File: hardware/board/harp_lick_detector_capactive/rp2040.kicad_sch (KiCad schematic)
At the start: 5 parts

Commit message: update analog front end
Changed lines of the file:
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@@
-    (effects (font (size 1.27 1.27)) (justify left))
-  )
-  (hierarchical_label "POCI" (shape input) (at 257.81 64.77 0)
     (effects (font (size 1.27 1.27)) (justify left))
   )
@@
     (effects (font (size 1.27 1.27)) (justify left))
   )
+  (hierarchical_label "ADC" (shape input) (at 257.81 125.73 0)
+    (effects (font (size 1.27 1.27)) (justify left))
+  )

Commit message: assign sch components partial
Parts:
- J2: renamed from J?; value USB_C_Receptacle_USB2.0 -> (none)
- R? (x2): value 5K1 -> (none)
- U7: renamed from U?; value W25Q128JVS -> (none); footprint Package_SO:SOIC-8_5.23x5.23mm_P1.27mm -> (none)
- U8: renamed from U?; value RP2040 -> (none); footprint RP2040_minimal:RP2040-QFN-56 -> (none)
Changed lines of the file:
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@@
     (in_bom yes) (on_board yes)
     (property "Reference" "R?" (id 0) (at 54.61 76.2 90))
-    (property "Value" "5K1" (id 1) (at 59.69 76.2 90))
+    (property "Value" "" (id 1) (at 59.69 76.2 90))
     (property "Footprint" "" (id 2) (at 57.15 80.518 90)
       (effects (font (size 1.27 1.27)) hide)
@@
   (symbol (lib_id "pi_pico:RP2040") (at 193.04 95.25 0) (unit 1)
     (in_bom yes) (on_board yes) (fields_autoplaced)
-    (property "Reference" "U?" (id 0) (at 195.0594 146.05 0)
+    (property "Reference" "U8" (id 0) (at 195.0594 146.05 0)
       (effects (font (size 1.27 1.27)) (justify left))
     )
-    (property "Value" "RP2040" (id 1) (at 195.0594 148.59 0)
+    (property "Value" "" (id 1) (at 195.0594 148.59 0)
       (effects (font (size 1.27 1.27)) (justify left))
     )
-    (property "Footprint" "RP2040_minimal:RP2040-QFN-56" (id 2) (at 173.99 95.25 0)
+    (property "Footprint" "" (id 2) (at 173.99 95.25 0)
       (effects (font (size 1.27 1.27)) hide)
     )
@@
   (symbol (lib_id "Memory_Flash:W25Q128JVS") (at 140.97 177.8 0) (unit 1)
     (in_bom yes) (on_board yes) (fields_autoplaced)
-    (property "Reference" "U?" (id 0) (at 142.9894 165.1 0)
+    (property "Reference" "U7" (id 0) (at 142.9894 165.1 0)
       (effects (font (size 1.27 1.27)) (justify left))
     )
-    (property "Value" "W25Q128JVS" (id 1) (at 142.9894 167.64 0)
+    (property "Value" "" (id 1) (at 142.9894 167.64 0)
       (effects (font (size 1.27 1.27)) (justify left))
     )
-    (property "Footprint" "Package_SO:SOIC-8_5.23x5.23mm_P1.27mm" (id 2) (at 140.97 177.8 0)
+    (property "Footprint" "" (id 2) (at 140.97 177.8 0)
       (effects (font (size 1.27 1.27)) hide)
     )
@@
   (symbol (lib_id "Connector:USB_C_Receptacle_USB2.0") (at 35.56 88.9 0) (unit 1)
     (in_bom yes) (on_board yes) (fields_autoplaced)
-    (property "Reference" "J?" (id 0) (at 35.56 66.04 0))
-    (property "Value" "USB_C_Receptacle_USB2.0" (id 1) (at 35.56 68.58 0))
+    (property "Reference" "J2" (id 0) (at 35.56 66.04 0))
+    (property "Value" "" (id 1) (at 35.56 68.58 0))
     (property "Footprint" "" (id 2) (at 39.37 88.9 0)
       (effects (font (size 1.27 1.27)) hide)
@@
     (in_bom yes) (on_board yes)
     (property "Reference" "R?" (id 0) (at 54.61 83.82 90))
-    (property "Value" "5K1" (id 1) (at 59.69 83.82 90))
+    (property "Value" "" (id 1) (at 59.69 83.82 90))
     (property "Footprint" "" (id 2) (at 57.15 83.058 90)
       (effects (font (size 1.27 1.27)) hide)

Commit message: assign more sch components
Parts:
- R? (x2): Link (none) -> https://www.digikey.com/en/products/detail/panasonic-electr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; Manufacturer (none) -> Panasonic Electronic Components; Manufacturer Number (none) -> ERJ-UP3F5101V; Tolerance (none) -> 1%
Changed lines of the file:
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@@
       (effects (font (size 1.27 1.27)) hide)
     )
-    (property "Datasheet" "~" (id 3) (at 57.15 78.74 0)
+    (property "Datasheet" "https://api.pim.na.industrial.panasonic.com/file_stream/main/fileversion/4484" (id 3) (at 57.15 78.74 0)
+      (effects (font (size 1.27 1.27)) hide)
+    )
+    (property "Link" "https://www.digikey.com/en/products/detail/panasonic-electronic-components/ERJ-UP3F5101V/12093051" (id 4) (at 57.15 78.74 0)
+      (effects (font (size 1.27 1.27)) hide)
+    )
+    (property "Manufacturer" "Panasonic Electronic Components" (id 5) (at 57.15 78.74 0)
+      (effects (font (size 1.27 1.27)) hide)
+    )
+    (property "Manufacturer Number" "ERJ-UP3F5101V" (id 6) (at 57.15 78.74 0)
+      (effects (font (size 1.27 1.27)) hide)
+    )
+    (property "Tolerance" "1%" (id 7) (at 57.15 78.74 0)
       (effects (font (size 1.27 1.27)) hide)
     )
@@
       (effects (font (size 1.27 1.27)) hide)
     )
-    (property "Datasheet" "~" (id 3) (at 57.15 81.28 0)
+    (property "Datasheet" "https://api.pim.na.industrial.panasonic.com/file_stream/main/fileversion/4484" (id 3) (at 57.15 81.28 0)
+      (effects (font (size 1.27 1.27)) hide)
+    )
+    (property "Link" "https://www.digikey.com/en/products/detail/panasonic-electronic-components/ERJ-UP3F5101V/12093051" (id 4) (at 57.15 81.28 0)
+      (effects (font (size 1.27 1.27)) hide)
+    )
+    (property "Manufacturer" "Panasonic Electronic Components" (id 5) (at 57.15 81.28 0)
+      (effects (font (size 1.27 1.27)) hide)
+    )
+    (property "Manufacturer Number" "ERJ-UP3F5101V" (id 6) (at 57.15 81.28 0)
+      (effects (font (size 1.27 1.27)) hide)
+    )
+    (property "Tolerance" "1%" (id 7) (at 57.15 81.28 0)
       (effects (font (size 1.27 1.27)) hide)
     )
@@
   (symbol (lib_id "power:VBUS") (at 52.07 72.39 0) (unit 1)
     (in_bom yes) (on_board yes) (fields_autoplaced)
-    (property "Reference" "#PWR?" (id 0) (at 52.07 76.2 0)
+    (property "Reference" "#PWR0135" (id 0) (at 52.07 76.2 0)
       (effects (font (size 1.27 1.27)) hide)
     )
@@
   (symbol (lib_id "power:GND") (at 63.5 80.01 90) (unit 1)
     (in_bom yes) (on_board yes) (fields_autoplaced)
-    (property "Reference" "#PWR?" (id 0) (at 69.85 80.01 0)
+    (property "Reference" "#PWR0134" (id 0) (at 69.85 80.01 0)
       (effects (font (size 1.27 1.27)) hide)
     )

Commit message: assign more components
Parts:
- added D?: (no value), symbol Device:LED
- added FID? (x3): (no value), symbol Mechanical:Fiducial
- J2: Link (none) -> https://www.digikey.com/en/products/detail/amphenol-cs-comm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; Manufacturer (none) -> Amphenol ICC (Commercial Products); Manufacturer Number (none) -> 12401610E4#2A
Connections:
- net GND: now also J2.A1 (GND), J2.A12 (GND), J2.B1 (GND), J2.B12 (GND), J2.S1 (SHIELD)
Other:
- note added: "TODO: crystal TODO: 3v3 Serial Port TODO: reset TODO: SWD port TODO: Harp audio jack TODO: USB Ground Loop Breaker"
- note removed: "TODO: Don't forget Fiducials."
- note removed: "TODO: crystal TODO: reset TODO: SWD port TODO: Harp audio jack"
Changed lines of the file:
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@@
   (junction (at 52.07 87.63) (diameter 0) (color 0 0 0 0)
+  )
+  (junction (at 31.75 113.03) (diameter 0) (color 0 0 0 0)
   )
   (junction (at 52.07 92.71) (diameter 0) (color 0 0 0 0)
@@
   (no_connect (at 50.8 101.6))
   (no_connect (at 50.8 104.14))
+  (wire (pts (xy 35.56 111.76) (xy 35.56 113.03))
+    (stroke (width 0) (type default) (color 0 0 0 0))
+  )
   (wire (pts (xy 60.96 78.74) (xy 62.23 78.74))
     (stroke (width 0) (type default) (color 0 0 0 0))
@@
     (stroke (width 0) (type default) (color 0 0 0 0))
   )
+  (wire (pts (xy 27.94 111.76) (xy 27.94 113.03))
+    (stroke (width 0) (type default) (color 0 0 0 0))
+  )
   (wire (pts (xy 52.07 93.98) (xy 50.8 93.98))
     (stroke (width 0) (type default) (color 0 0 0 0))
@@
     (stroke (width 0) (type default) (color 0 0 0 0))
   )
+  (wire (pts (xy 35.56 113.03) (xy 31.75 113.03))
+    (stroke (width 0) (type default) (color 0 0 0 0))
+  )
   (wire (pts (xy 62.23 81.28) (xy 62.23 80.01))
     (stroke (width 0) (type default) (color 0 0 0 0))
@@
     (stroke (width 0) (type default) (color 0 0 0 0))
   )
+  (wire (pts (xy 27.94 113.03) (xy 31.75 113.03))
+    (stroke (width 0) (type default) (color 0 0 0 0))
+  )
   (wire (pts (xy 52.07 72.39) (xy 52.07 73.66))
     (stroke (width 0) (type default) (color 0 0 0 0))
@@
     (stroke (width 0) (type default) (color 0 0 0 0))
   )
+  (wire (pts (xy 31.75 113.03) (xy 31.75 114.3))
+    (stroke (width 0) (type default) (color 0 0 0 0))
+  )
   (wire (pts (xy 50.8 86.36) (xy 52.07 86.36))
     (stroke (width 0) (type default) (color 0 0 0 0))
@@
     (stroke (width 0) (type default) (color 0 0 0 0))
   )
-  (text "TODO: crystal\nTODO: reset\nTODO: SWD port\nTODO: Harp audio jack"
+  (text "TODO: crystal\nTODO: 3v3 Serial Port\nTODO: reset\nTODO: SWD port\nTODO: Harp audio jack\nTODO: USB Ground Loop Breaker"
     (at 20.32 184.15 0)
-    (effects (font (size 1.27 1.27)) (justify left bottom))
-  )
-  (text "TODO: Don't forget Fiducials." (at 251.46 17.78 0)
     (effects (font (size 1.27 1.27)) (justify left bottom))
   )
@@
     (pin "1")
     (pin "2")
+  )
+  (symbol (lib_id "power:GND") (at 31.75 114.3 0) (unit 1)
+    (in_bom yes) (on_board yes) (fields_autoplaced)
+    (property "Reference" "#PWR?" (id 0) (at 31.75 120.65 0)
+      (effects (font (size 1.27 1.27)) hide)
+    )
+    (property "Value" "GND" (id 1) (at 34.29 115.5699 0)
+      (effects (font (size 1.27 1.27)) (justify left))
+    )
+    (property "Footprint" "" (id 2) (at 31.75 114.3 0)
+      (effects (font (size 1.27 1.27)) hide)
+    )
+    (property "Datasheet" "" (id 3) (at 31.75 114.3 0)
+      (effects (font (size 1.27 1.27)) hide)
+    )
+    (pin "1")
   )
   (symbol (lib_id "pi_pico:RP2040") (at 193.04 95.25 0) (unit 1)
@@
     (pin "9")
   )
+  (symbol (lib_id "Mechanical:Fiducial") (at 17.78 24.13 0) (unit 1)
+    (in_bom yes) (on_board yes) (fields_autoplaced)
+    (property "Reference" "FID?" (id 0) (at 20.32 22.8599 0)
+      (effects (font (size 1.27 1.27)) (justify left))
+    )
+    (property "Value" "" (id 1) (at 20.32 25.3999 0)
+      (effects (font (size 1.27 1.27)) (justify left))
+    )
+    (property "Footprint" "" (id 2) (at 17.78 24.13 0)
+      (effects (font (size 1.27 1.27)) hide)
+    )
+    (property "Datasheet" "~" (id 3) (at 17.78 24.13 0)
+      (effects (font (size 1.27 1.27)) hide)
+    )
+  )
+  (symbol (lib_id "Mechanical:Fiducial") (at 17.78 29.21 0) (unit 1)
+    (in_bom yes) (on_board yes) (fields_autoplaced)
+    (property "Reference" "FID?" (id 0) (at 20.32 27.9399 0)
+      (effects (font (size 1.27 1.27)) (justify left))
+    )
+    (property "Value" "" (id 1) (at 20.32 30.4799 0)
+      (effects (font (size 1.27 1.27)) (justify left))
+    )
+    (property "Footprint" "" (id 2) (at 17.78 29.21 0)
+      (effects (font (size 1.27 1.27)) hide)
+    )
+    (property "Datasheet" "~" (id 3) (at 17.78 29.21 0)
+      (effects (font (size 1.27 1.27)) hide)
+    )
+  )
   (symbol (lib_id "Memory_Flash:W25Q128JVS") (at 140.97 177.8 0) (unit 1)
     (in_bom yes) (on_board yes) (fields_autoplaced)
@@
     )
     (property "Datasheet" "https://www.usb.org/sites/default/files/documents/usb_type-c.zip" (id 3) (at 39.37 88.9 0)
+      (effects (font (size 1.27 1.27)) hide)
+    )
+    (property "Link" "https://www.digikey.com/en/products/detail/amphenol-cs-commercial-products/12401610E4-2A/5775519" (id 4) (at 35.56 88.9 0)
+      (effects (font (size 1.27 1.27)) hide)
+    )
+    (property "Manufacturer" "Amphenol ICC (Commercial Products)" (id 5) (at 35.56 88.9 0)
+      (effects (font (size 1.27 1.27)) hide)
+    )
+    (property "Manufacturer Number" "12401610E4#2A" (id 6) (at 35.56 88.9 0)
       (effects (font (size 1.27 1.27)) hide)
     )
@@
     (pin "1")
   )
+  (symbol (lib_id "Mechanical:Fiducial") (at 17.78 19.05 0) (unit 1)
+    (in_bom yes) (on_board yes) (fields_autoplaced)
+    (property "Reference" "FID?" (id 0) (at 20.32 17.7799 0)
+      (effects (font (size 1.27 1.27)) (justify left))
+    )
+    (property "Value" "" (id 1) (at 20.32 20.3199 0)
+      (effects (font (size 1.27 1.27)) (justify left))
+    )
+    (property "Footprint" "" (id 2) (at 17.78 19.05 0)
+      (effects (font (size 1.27 1.27)) hide)
+    )
+    (property "Datasheet" "~" (id 3) (at 17.78 19.05 0)
+      (effects (font (size 1.27 1.27)) hide)
+    )
+  )
   (symbol (lib_id "power:GND") (at 63.5 80.01 90) (unit 1)
     (in_bom yes) (on_board yes) (fields_autoplaced)
@@
     (pin "1")
   )
+  (symbol (lib_id "Device:LED") (at 270.51 81.28 90) (unit 1)
+    (in_bom yes) (on_board yes) (fields_autoplaced)
+    (property "Reference" "D?" (id 0) (at 274.32 81.5974 90)
+      (effects (font (size 1.27 1.27)) (justify right))
+    )
+    (property "Value" "" (id 1) (at 274.32 84.1374 90)
+      (effects (font (size 1.27 1.27)) (justify right))
+    )
+    (property "Footprint" "" (id 2) (at 270.51 81.28 0)
+      (effects (font (size 1.27 1.27)) hide)
+    )
+    (property "Datasheet" "~" (id 3) (at 270.51 81.28 0)
+      (effects (font (size 1.27 1.27)) hide)
+    )
+    (pin "1")
+    (pin "2")
+  )
 )

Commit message: assign more components
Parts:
- U7: Link (none) -> https://www.digikey.com/en/products/detail/winbond-electron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; Manufacturer (none) -> Winbond Electronics; Manufacturer Number (none) -> W25Q128JVSIQ TR
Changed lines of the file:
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@@
+      (effects (font (size 1.27 1.27)) hide)
+    )
+    (property "Link" "https://www.digikey.com/en/products/detail/winbond-electronics/W25Q128JVSIQ-TR/5803944" (id 4) (at 140.97 177.8 0)
+      (effects (font (size 1.27 1.27)) hide)
+    )
+    (property "Manufacturer" "Winbond Electronics" (id 5) (at 140.97 177.8 0)
+      (effects (font (size 1.27 1.27)) hide)
+    )
+    (property "Manufacturer Number" "W25Q128JVSIQ TR" (id 6) (at 140.97 177.8 0)
       (effects (font (size 1.27 1.27)) hide)
     )

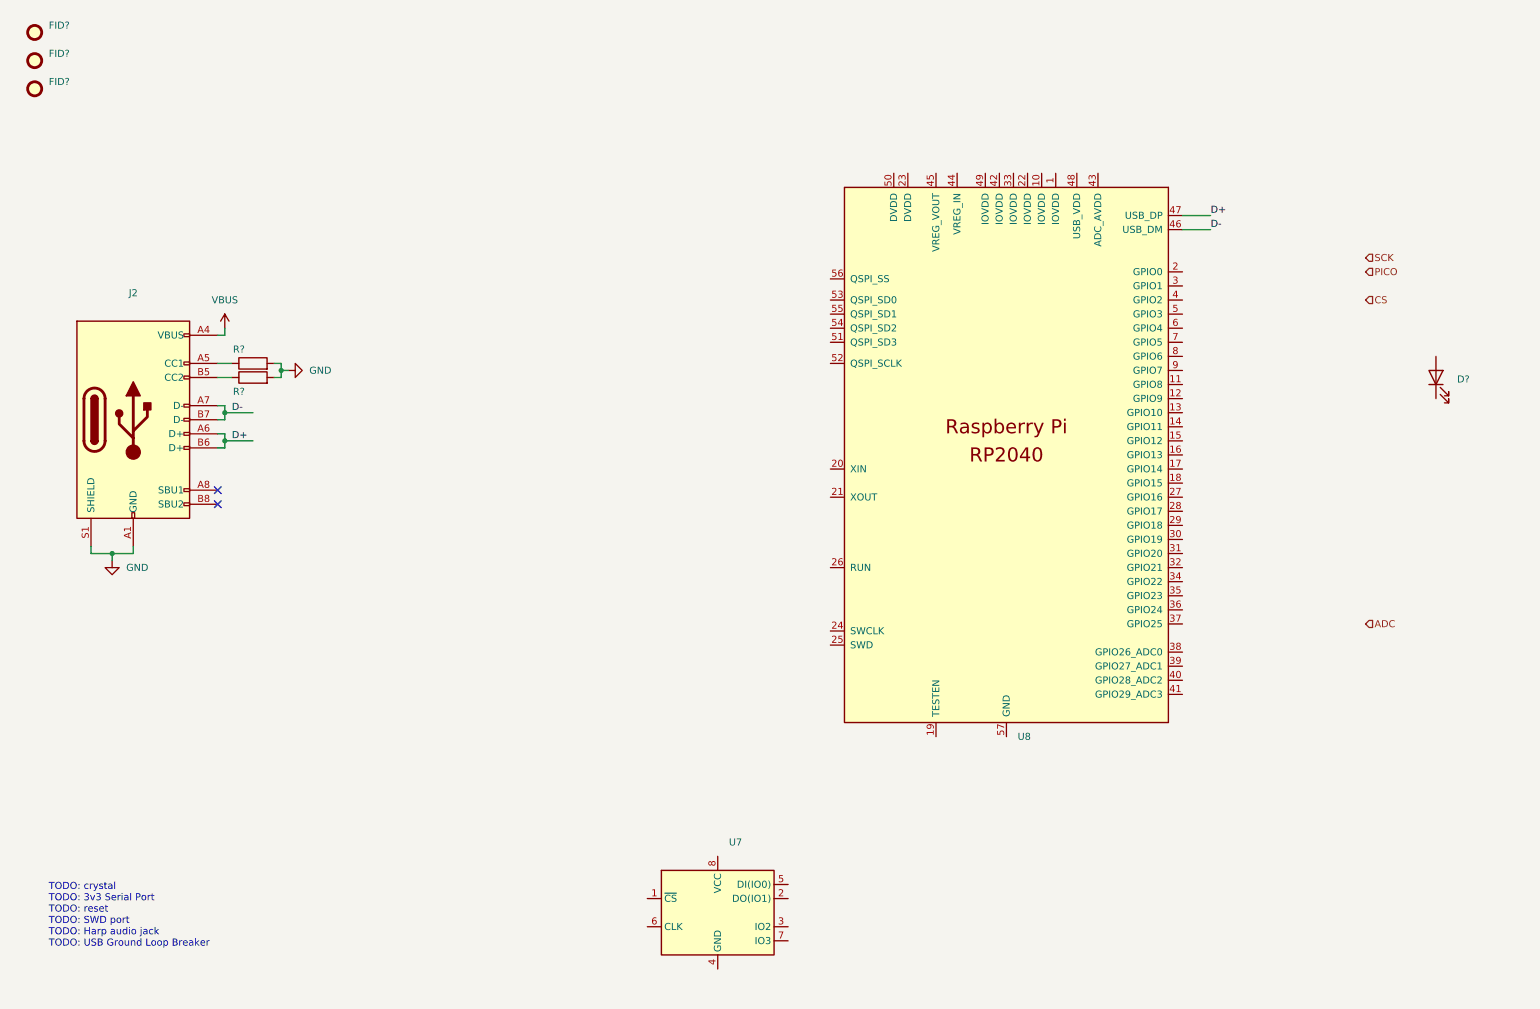
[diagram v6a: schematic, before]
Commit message: add precision oscillator
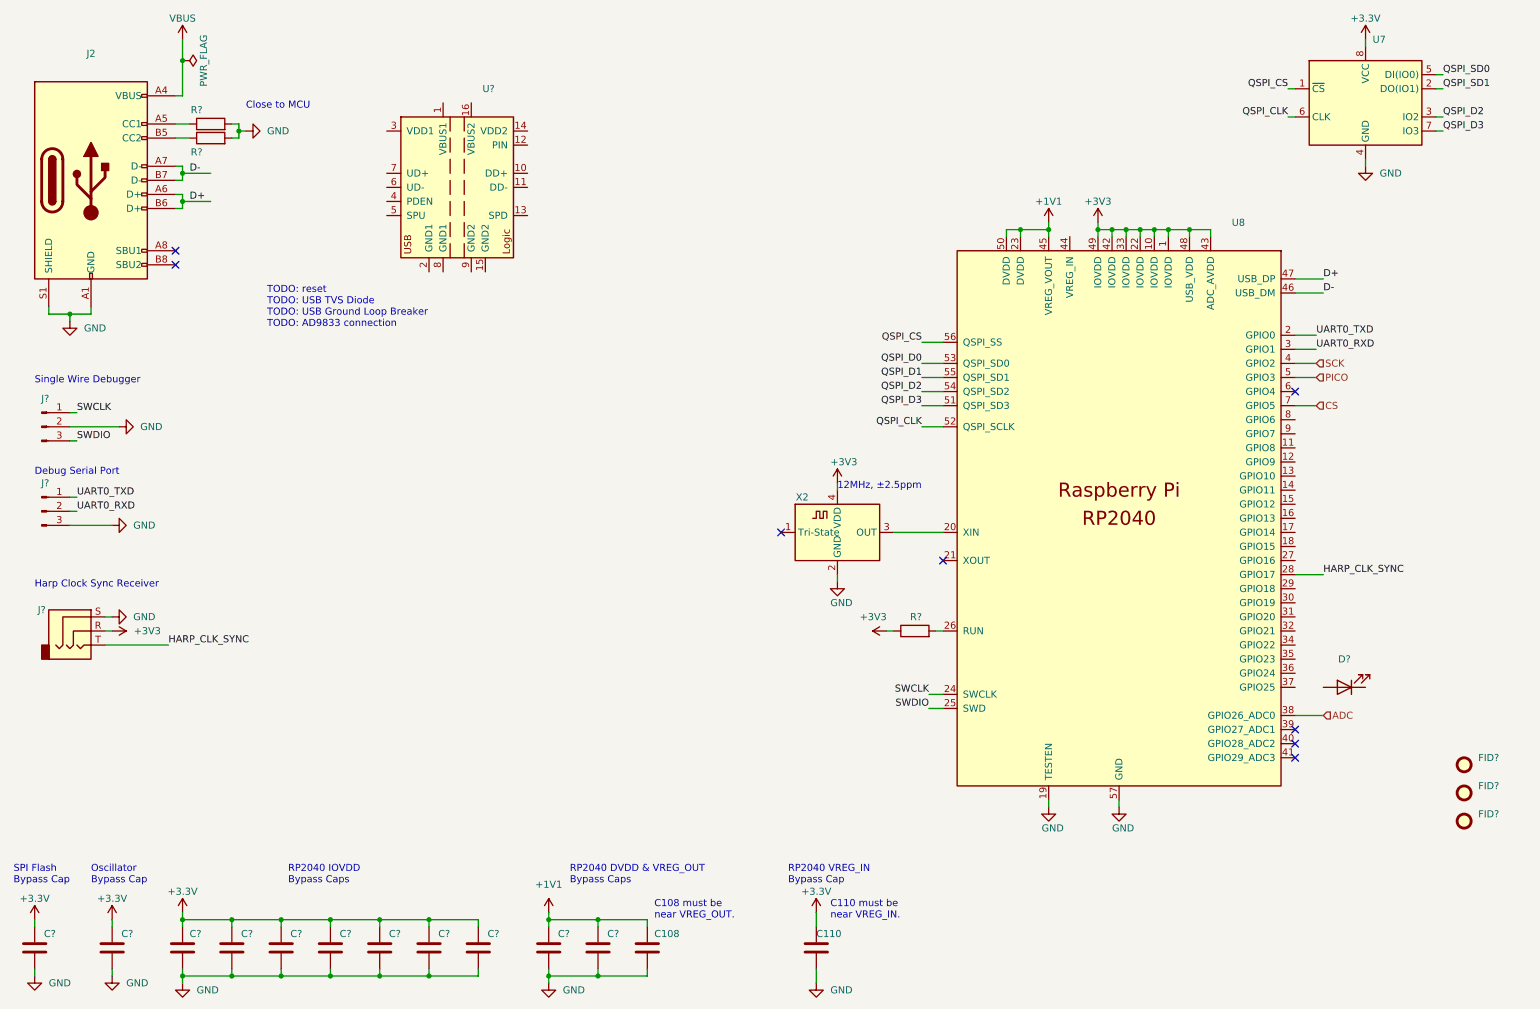
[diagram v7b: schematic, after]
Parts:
- added C108, C110, C? (x11): (no value), symbol Device:C
- added J?: (no value), symbol Connector:AudioJack3
- added J? (x2): (no value), symbol Connector:Conn_01x03_Male
- added R?: (no value), symbol Device:R
- added U?: (no value), symbol Interface_USB:ADUM4160
- added X2: (no value), symbol machine_agency_components:ECS-TXO-2016
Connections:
- net ADC: now also U8.38 (GPIO26_ADC0)
- net CS: now also U8.7 (GPIO5)
- net GND: now also U7.4 (GND), U8.19 (TESTEN), U8.57 (GND), C108.2, C110.2, C?.1, C?.1, C?.1, C?.1, C?.1, C?.1, C?.1, C?.1, C?.1, C?.1, C?.2, J?.2 (Pin_2), J?.3 (Pin_3), J?.S, X2.2 (GND)
- net PICO: now also U8.5 (GPIO3)
- net SCK: now also U8.4 (GPIO2)
- net +3V3: now reaches U8.1 (IOVDD)
- net +3V3: now also U7.8 (VCC), U8.10 (IOVDD), U8.22 (IOVDD), U8.33 (IOVDD), U8.42 (IOVDD), U8.43 (ADC_AVDD), U8.48 (USB_VDD), U8.49 (IOVDD), C110.1, C?.1, C?.2, C?.2, C?.2, C?.2, C?.2, C?.2, C?.2, C?.2, J?.R, R?.1, X2.4 (VDD)
- net UART0_TXD: now reaches U8.2 (GPIO0)
- net UART0_TXD: now also J?.1 (Pin_1)
- net at U8.20 (XIN): now also X2.3 (OUT)
- net +1V1: now reaches U8.23 (DVDD)
- net +1V1: now also U8.45 (VREG_VOUT), U8.50 (DVDD), C108.1, C?.2, C?.2
- net SWCLK: now reaches U8.24 (SWCLK)
- net SWCLK: now also J?.1 (Pin_1)
- net SWDIO: now reaches U8.25 (SWD)
- net SWDIO: now also J?.3 (Pin_3)
- net at U8.26 (RUN): now also R?.2
- net HARP_CLK_SYNC: now reaches U8.28 (GPIO17)
- net HARP_CLK_SYNC: now also J?.T
- net UART0_RXD: now reaches U8.3 (GPIO1)
- net UART0_RXD: now also J?.2 (Pin_2)
- net QSPI_D3: now reaches U8.51 (QSPI_SD3)
- net QSPI_D3: now also U7.7 (IO3)
- net QSPI_CLK: now reaches U8.52 (QSPI_SCLK)
- net QSPI_CLK: now also U7.6 (CLK)
- net QSPI_D0: now reaches U8.53 (QSPI_SD0)
- net QSPI_D2: now reaches U8.54 (QSPI_SD2)
- net QSPI_D2: now also U7.3 (IO2)
- net QSPI_D1: now reaches U8.55 (QSPI_SD1)
- net QSPI_CS: now reaches U8.56 (QSPI_SS)
- net QSPI_CS: now also U7.1 (~{CS})
- net QSPI_SD1: now reaches U7.2 (DO(IO1))
- net QSPI_SD0: now reaches U7.5 (DI(IO0))
- no-connect marks 2 -> 8
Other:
- note added: "12MHz, ±2.5ppm"
- note added: "C108 must be near VREG_OUT."
- note added: "C110 must be near VREG_IN."
- note added: "Close to MCU"
- note added: "Debug Serial Port"
- note added: "Harp Clock Sync Receiver"
- note added: "Oscillator Bypass Cap"
- note added: "RP2040 DVDD & VREG_OUT Bypass Caps"
- note added: "RP2040 IOVDD Bypass Caps"
- note added: "RP2040 VREG_IN Bypass Cap"
- note added: "SPI Flash Bypass Cap"
- note added: "Single Wire Debugger"
- note added: "TODO: reset TODO: USB TVS Diode TODO: USB Ground Loop Breaker TODO: AD9833 connection"
- note removed: "TODO: crystal TODO: 3v3 Serial Port TODO: reset TODO: SWD port TODO: Harp audio jack TODO: USB Ground Loop Breaker"
- moved on the sheet: D?, FID?, J2, R?, U7, U8
